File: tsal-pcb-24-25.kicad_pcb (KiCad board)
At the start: 2 copper layers, 87.6 x 36.8 mm, 30 parts, among them J1 043045-0412, Q1 DMP2035U-7, Q3 UJ3N065080K3S, Q4 DMN2056U, U1 H11L1M, U2 NE555D

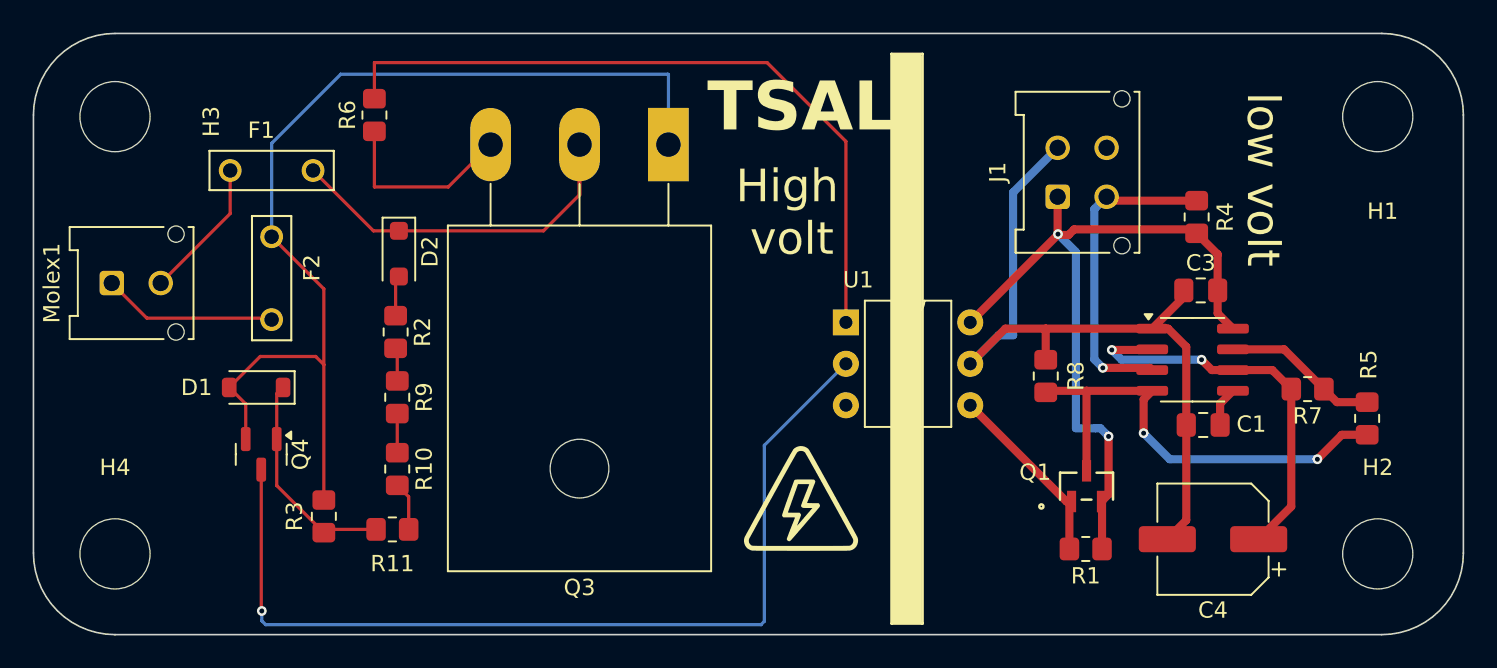
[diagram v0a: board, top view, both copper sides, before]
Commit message: updated pcb-24-25 to have new sch and applied to pcb
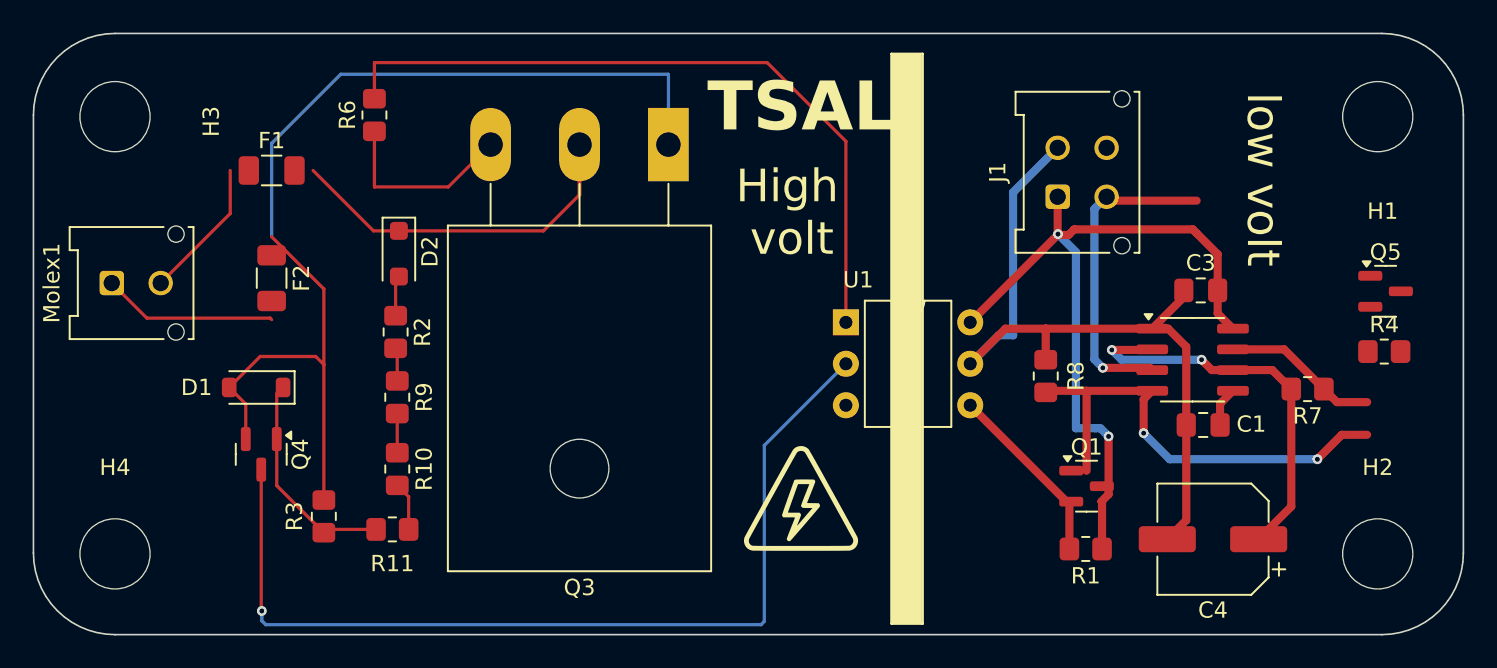
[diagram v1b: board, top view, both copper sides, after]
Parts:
- removed R5: 100, Resistor_SMD:R_0805_2012Metric_Pad1.20x1.40mm_HandSolder
- added Q5: AO3401A, Package_TO_SOT_SMD:SOT-23, F.Cu at (192.1, 95.8)
- F1, F2: footprint Library:FUSE_BK_PCS -> Fuse:Fuse_1206_3216Metric
- Q1: footprint Package_TO_SOT_SMD:SOT23_DIO -> Package_TO_SOT_SMD:SOT-23
- R4: value 1k -> 5k
- moved R4 14.2 mm to (192.0, 99.5), turned to 0 degrees
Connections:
- R4 pad 2: Light+ -> unconnected-(Q5-G-Pad1)
- R7 pad 1: Net-(U2-DIS) -> Net-(U2-THR)
- R7 pad 2: Net-(U2-THR) -> unconnected-(Q5-G-Pad1)
- U2 pad 3: Light+ -> unconnected-(Q5-G-Pad1)
- U2 pad 7: Net-(U2-DIS) -> unconnected-(Q5-G-Pad1)
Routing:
- net Net-(U2-DIS): track 9.56 -> 0.00 mm
- net (no net): track 0.00 -> 9.56 mm
